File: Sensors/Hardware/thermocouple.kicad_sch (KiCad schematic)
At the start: 8 parts, among them U18 MAX31856

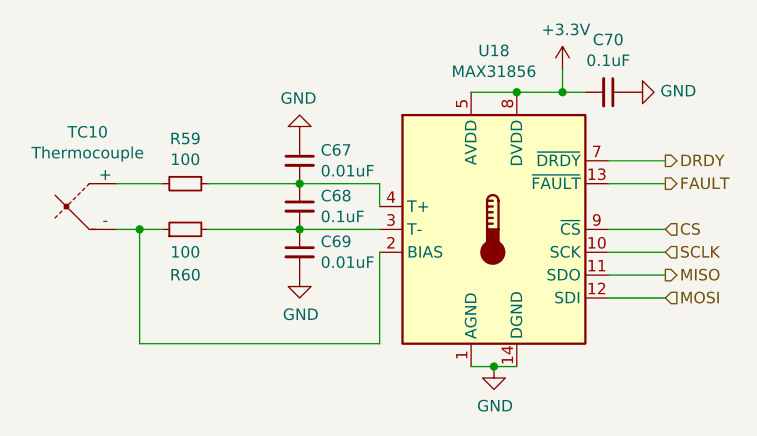
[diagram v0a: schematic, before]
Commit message: added new ADC and some connections
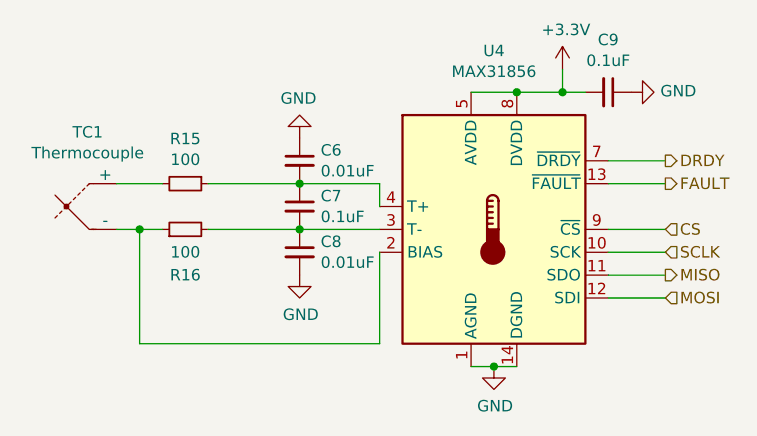
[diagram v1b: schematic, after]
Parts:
- renumbered C67 to C6, C68 to C7, C69 to C8, C70 to C9, R59 to R15, R60 to R16, TC10 to TC1, U18 to U4
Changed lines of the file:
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@@
   (symbol (lib_id "Sensor_Temperature:MAX31856") (at 95.25 73.66 0)
     (in_bom yes) (on_board yes)
-    (property "Reference" "U18" (id 0) (at 95.25 53.8226 0))
+    (property "Reference" "U4" (id 0) (at 95.25 53.8226 0))
     (property "Value" "MAX31856" (id 1) (at 95.25 56.134 0))
     (property "Footprint" "Package_SO:TSSOP-14_4.4x5mm_P0.65mm" (id 2) (at 99.06 87.63 0)
@@
   (symbol (lib_id "power:GND") (at 95.25 88.9 0)
     (in_bom yes) (on_board yes)
-    (property "Reference" "#PWR0130" (id 0) (at 95.25 95.25 0)
+    (property "Reference" "#PWR026" (id 0) (at 95.25 95.25 0)
       (effects (font (size 1.27 1.27)) hide)
     )
@@
   (symbol (lib_id "analogue-cache:+3.3V") (at 102.87 55.88 0)
     (in_bom yes) (on_board yes)
-    (property "Reference" "#PWR0131" (id 0) (at 102.87 59.69 0)
+    (property "Reference" "#PWR028" (id 0) (at 102.87 59.69 0)
       (effects (font (size 1.27 1.27)) hide)
     )
@@
   (symbol (lib_id "Device:C_Small") (at 107.95 58.42 270)
     (in_bom yes) (on_board yes)
-    (property "Reference" "C70" (id 0) (at 107.95 52.6034 90))
+    (property "Reference" "C9" (id 0) (at 107.95 52.6034 90))
     (property "Value" "0.1uF" (id 1) (at 107.95 54.9148 90))
     (property "Footprint" "Capacitor_SMD:C_0603_1608Metric" (id 2) (at 107.95 58.42 0)
@@
   (symbol (lib_id "power:GND") (at 110.49 58.42 90)
     (in_bom yes) (on_board yes)
-    (property "Reference" "#PWR0132" (id 0) (at 116.84 58.42 0)
+    (property "Reference" "#PWR029" (id 0) (at 116.84 58.42 0)
       (effects (font (size 1.27 1.27)) hide)
     )
@@
   (symbol (lib_id "Device:Thermocouple") (at 50.8 71.12 0)
     (in_bom yes) (on_board yes)
-    (property "Reference" "TC10" (id 0) (at 50.1142 62.865 0))
+    (property "Reference" "TC1" (id 0) (at 50.1142 62.865 0))
     (property "Value" "Thermocouple" (id 1) (at 50.1142 65.1764 0))
     (property "Footprint" "TerminalBlock_TE-Connectivity:TerminalBlock_TE_282834-2_1x02_P2.54mm_Horizontal" (id 2) (at 36.195 69.85 0)
@@
   (symbol (lib_id "Device:R_Small") (at 60.96 68.58 270)
     (in_bom yes) (on_board yes)
-    (property "Reference" "R59" (id 0) (at 60.96 63.6016 90))
+    (property "Reference" "R15" (id 0) (at 60.96 63.6016 90))
     (property "Value" "100" (id 1) (at 60.96 65.913 90))
     (property "Footprint" "Resistor_SMD:R_0603_1608Metric" (id 2) (at 60.96 68.58 0)
@@
   (symbol (lib_id "Device:R_Small") (at 60.96 73.66 90)
     (in_bom yes) (on_board yes)
-    (property "Reference" "R60" (id 0) (at 60.96 78.74 90))
+    (property "Reference" "R16" (id 0) (at 60.96 78.74 90))
     (property "Value" "100" (id 1) (at 60.96 76.2 90))
     (property "Footprint" "Resistor_SMD:R_0603_1608Metric" (id 2) (at 60.96 73.66 0)
@@
   (symbol (lib_id "Device:C_Small") (at 73.66 71.12 0)
     (in_bom yes) (on_board yes)
-    (property "Reference" "C68" (id 0) (at 75.9968 69.9516 0)
+    (property "Reference" "C7" (id 0) (at 75.9968 69.9516 0)
       (effects (font (size 1.27 1.27)) (justify left))
     )
@@
   (symbol (lib_id "Device:C_Small") (at 73.66 66.04 0)
     (in_bom yes) (on_board yes)
-    (property "Reference" "C67" (id 0) (at 75.9968 64.8716 0)
+    (property "Reference" "C6" (id 0) (at 75.9968 64.8716 0)
       (effects (font (size 1.27 1.27)) (justify left))
     )
@@
   (symbol (lib_id "Device:C_Small") (at 73.66 76.2 0)
     (in_bom yes) (on_board yes)
-    (property "Reference" "C69" (id 0) (at 75.9968 75.0316 0)
+    (property "Reference" "C8" (id 0) (at 75.9968 75.0316 0)
       (effects (font (size 1.27 1.27)) (justify left))
     )
@@
   (symbol (lib_id "power:GND") (at 73.66 78.74 0)
     (in_bom yes) (on_board yes)
-    (property "Reference" "#PWR0129" (id 0) (at 73.66 85.09 0)
+    (property "Reference" "#PWR025" (id 0) (at 73.66 85.09 0)
       (effects (font (size 1.27 1.27)) hide)
     )
@@
   (symbol (lib_id "power:GND") (at 73.66 63.5 180)
     (in_bom yes) (on_board yes)
-    (property "Reference" "#PWR0128" (id 0) (at 73.66 57.15 0)
+    (property "Reference" "#PWR024" (id 0) (at 73.66 57.15 0)
       (effects (font (size 1.27 1.27)) hide)
     )

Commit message: connectors and update
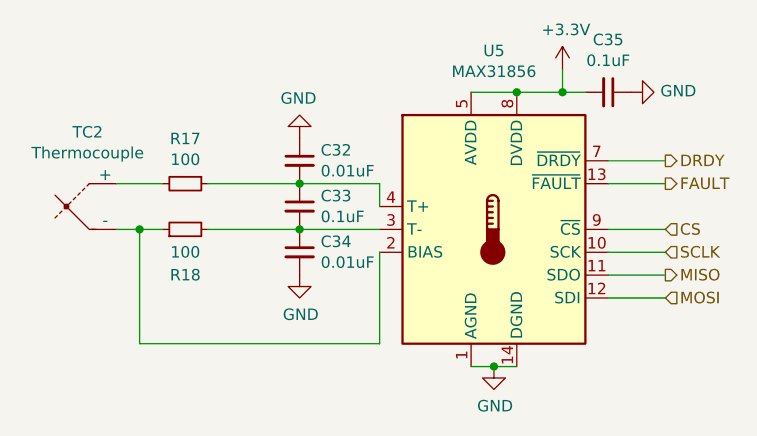
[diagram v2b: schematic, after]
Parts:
- renumbered C6 to C32, C7 to C33, C8 to C34, C9 to C35, R15 to R17, R16 to R18, TC1 to TC2, U4 to U5
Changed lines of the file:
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@@
   (symbol (lib_id "Sensor_Temperature:MAX31856") (at 95.25 73.66 0)
     (in_bom yes) (on_board yes)
-    (property "Reference" "U4" (id 0) (at 95.25 53.8226 0))
+    (property "Reference" "U5" (id 0) (at 95.25 53.8226 0))
     (property "Value" "MAX31856" (id 1) (at 95.25 56.134 0))
     (property "Footprint" "Package_SO:TSSOP-14_4.4x5mm_P0.65mm" (id 2) (at 99.06 87.63 0)
@@
   (symbol (lib_id "power:GND") (at 95.25 88.9 0)
     (in_bom yes) (on_board yes)
-    (property "Reference" "#PWR026" (id 0) (at 95.25 95.25 0)
+    (property "Reference" "#PWR032" (id 0) (at 95.25 95.25 0)
       (effects (font (size 1.27 1.27)) hide)
     )
@@
   (symbol (lib_id "analogue-cache:+3.3V") (at 102.87 55.88 0)
     (in_bom yes) (on_board yes)
-    (property "Reference" "#PWR028" (id 0) (at 102.87 59.69 0)
+    (property "Reference" "#PWR033" (id 0) (at 102.87 59.69 0)
       (effects (font (size 1.27 1.27)) hide)
     )
@@
   (symbol (lib_id "Device:C_Small") (at 107.95 58.42 270)
     (in_bom yes) (on_board yes)
-    (property "Reference" "C9" (id 0) (at 107.95 52.6034 90))
+    (property "Reference" "C35" (id 0) (at 107.95 52.6034 90))
     (property "Value" "0.1uF" (id 1) (at 107.95 54.9148 90))
     (property "Footprint" "Capacitor_SMD:C_0603_1608Metric" (id 2) (at 107.95 58.42 0)
@@
   (symbol (lib_id "power:GND") (at 110.49 58.42 90)
     (in_bom yes) (on_board yes)
-    (property "Reference" "#PWR029" (id 0) (at 116.84 58.42 0)
+    (property "Reference" "#PWR034" (id 0) (at 116.84 58.42 0)
       (effects (font (size 1.27 1.27)) hide)
     )
@@
   (symbol (lib_id "Device:Thermocouple") (at 50.8 71.12 0)
     (in_bom yes) (on_board yes)
-    (property "Reference" "TC1" (id 0) (at 50.1142 62.865 0))
+    (property "Reference" "TC2" (id 0) (at 50.1142 62.865 0))
     (property "Value" "Thermocouple" (id 1) (at 50.1142 65.1764 0))
     (property "Footprint" "TerminalBlock_TE-Connectivity:TerminalBlock_TE_282834-2_1x02_P2.54mm_Horizontal" (id 2) (at 36.195 69.85 0)
@@
   (symbol (lib_id "Device:R_Small") (at 60.96 68.58 270)
     (in_bom yes) (on_board yes)
-    (property "Reference" "R15" (id 0) (at 60.96 63.6016 90))
+    (property "Reference" "R17" (id 0) (at 60.96 63.6016 90))
     (property "Value" "100" (id 1) (at 60.96 65.913 90))
     (property "Footprint" "Resistor_SMD:R_0603_1608Metric" (id 2) (at 60.96 68.58 0)
@@
   (symbol (lib_id "Device:R_Small") (at 60.96 73.66 90)
     (in_bom yes) (on_board yes)
-    (property "Reference" "R16" (id 0) (at 60.96 78.74 90))
+    (property "Reference" "R18" (id 0) (at 60.96 78.74 90))
     (property "Value" "100" (id 1) (at 60.96 76.2 90))
     (property "Footprint" "Resistor_SMD:R_0603_1608Metric" (id 2) (at 60.96 73.66 0)
@@
   (symbol (lib_id "Device:C_Small") (at 73.66 71.12 0)
     (in_bom yes) (on_board yes)
-    (property "Reference" "C7" (id 0) (at 75.9968 69.9516 0)
+    (property "Reference" "C33" (id 0) (at 75.9968 69.9516 0)
       (effects (font (size 1.27 1.27)) (justify left))
     )
@@
   (symbol (lib_id "Device:C_Small") (at 73.66 66.04 0)
     (in_bom yes) (on_board yes)
-    (property "Reference" "C6" (id 0) (at 75.9968 64.8716 0)
+    (property "Reference" "C32" (id 0) (at 75.9968 64.8716 0)
       (effects (font (size 1.27 1.27)) (justify left))
     )
@@
   (symbol (lib_id "Device:C_Small") (at 73.66 76.2 0)
     (in_bom yes) (on_board yes)
-    (property "Reference" "C8" (id 0) (at 75.9968 75.0316 0)
+    (property "Reference" "C34" (id 0) (at 75.9968 75.0316 0)
       (effects (font (size 1.27 1.27)) (justify left))
     )
@@
   (symbol (lib_id "power:GND") (at 73.66 78.74 0)
     (in_bom yes) (on_board yes)
-    (property "Reference" "#PWR025" (id 0) (at 73.66 85.09 0)
+    (property "Reference" "#PWR031" (id 0) (at 73.66 85.09 0)
       (effects (font (size 1.27 1.27)) hide)
     )
@@
   (symbol (lib_id "power:GND") (at 73.66 63.5 180)
     (in_bom yes) (on_board yes)
-    (property "Reference" "#PWR024" (id 0) (at 73.66 57.15 0)
+    (property "Reference" "#PWR030" (id 0) (at 73.66 57.15 0)
       (effects (font (size 1.27 1.27)) hide)
     )

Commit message: potential divider preliminary
for connectors
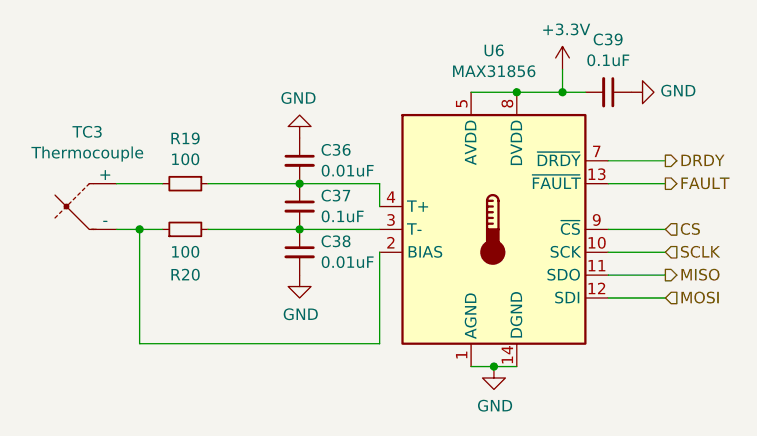
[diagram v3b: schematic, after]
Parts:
- renumbered C32 to C36, C33 to C37, C34 to C38, C35 to C39, R17 to R19, R18 to R20, TC2 to TC3, U5 to U6
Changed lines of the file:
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@@
   (symbol (lib_id "Sensor_Temperature:MAX31856") (at 95.25 73.66 0)
     (in_bom yes) (on_board yes)
-    (property "Reference" "U5" (id 0) (at 95.25 53.8226 0))
+    (property "Reference" "U6" (id 0) (at 95.25 53.8226 0))
     (property "Value" "MAX31856" (id 1) (at 95.25 56.134 0))
     (property "Footprint" "Package_SO:TSSOP-14_4.4x5mm_P0.65mm" (id 2) (at 99.06 87.63 0)
@@
   (symbol (lib_id "power:GND") (at 95.25 88.9 0)
     (in_bom yes) (on_board yes)
-    (property "Reference" "#PWR032" (id 0) (at 95.25 95.25 0)
+    (property "Reference" "#PWR037" (id 0) (at 95.25 95.25 0)
       (effects (font (size 1.27 1.27)) hide)
     )
@@
   (symbol (lib_id "analogue-cache:+3.3V") (at 102.87 55.88 0)
     (in_bom yes) (on_board yes)
-    (property "Reference" "#PWR033" (id 0) (at 102.87 59.69 0)
+    (property "Reference" "#PWR038" (id 0) (at 102.87 59.69 0)
       (effects (font (size 1.27 1.27)) hide)
     )
@@
   (symbol (lib_id "Device:C_Small") (at 107.95 58.42 270)
     (in_bom yes) (on_board yes)
-    (property "Reference" "C35" (id 0) (at 107.95 52.6034 90))
+    (property "Reference" "C39" (id 0) (at 107.95 52.6034 90))
     (property "Value" "0.1uF" (id 1) (at 107.95 54.9148 90))
     (property "Footprint" "Capacitor_SMD:C_0603_1608Metric" (id 2) (at 107.95 58.42 0)
@@
   (symbol (lib_id "power:GND") (at 110.49 58.42 90)
     (in_bom yes) (on_board yes)
-    (property "Reference" "#PWR034" (id 0) (at 116.84 58.42 0)
+    (property "Reference" "#PWR039" (id 0) (at 116.84 58.42 0)
       (effects (font (size 1.27 1.27)) hide)
     )
@@
   (symbol (lib_id "Device:Thermocouple") (at 50.8 71.12 0)
     (in_bom yes) (on_board yes)
-    (property "Reference" "TC2" (id 0) (at 50.1142 62.865 0))
+    (property "Reference" "TC3" (id 0) (at 50.1142 62.865 0))
     (property "Value" "Thermocouple" (id 1) (at 50.1142 65.1764 0))
     (property "Footprint" "TerminalBlock_TE-Connectivity:TerminalBlock_TE_282834-2_1x02_P2.54mm_Horizontal" (id 2) (at 36.195 69.85 0)
@@
   (symbol (lib_id "Device:R_Small") (at 60.96 68.58 270)
     (in_bom yes) (on_board yes)
-    (property "Reference" "R17" (id 0) (at 60.96 63.6016 90))
+    (property "Reference" "R19" (id 0) (at 60.96 63.6016 90))
     (property "Value" "100" (id 1) (at 60.96 65.913 90))
     (property "Footprint" "Resistor_SMD:R_0603_1608Metric" (id 2) (at 60.96 68.58 0)
@@
   (symbol (lib_id "Device:R_Small") (at 60.96 73.66 90)
     (in_bom yes) (on_board yes)
-    (property "Reference" "R18" (id 0) (at 60.96 78.74 90))
+    (property "Reference" "R20" (id 0) (at 60.96 78.74 90))
     (property "Value" "100" (id 1) (at 60.96 76.2 90))
     (property "Footprint" "Resistor_SMD:R_0603_1608Metric" (id 2) (at 60.96 73.66 0)
@@
   (symbol (lib_id "Device:C_Small") (at 73.66 71.12 0)
     (in_bom yes) (on_board yes)
-    (property "Reference" "C33" (id 0) (at 75.9968 69.9516 0)
+    (property "Reference" "C37" (id 0) (at 75.9968 69.9516 0)
       (effects (font (size 1.27 1.27)) (justify left))
     )
@@
   (symbol (lib_id "Device:C_Small") (at 73.66 66.04 0)
     (in_bom yes) (on_board yes)
-    (property "Reference" "C32" (id 0) (at 75.9968 64.8716 0)
+    (property "Reference" "C36" (id 0) (at 75.9968 64.8716 0)
       (effects (font (size 1.27 1.27)) (justify left))
     )
@@
   (symbol (lib_id "Device:C_Small") (at 73.66 76.2 0)
     (in_bom yes) (on_board yes)
-    (property "Reference" "C34" (id 0) (at 75.9968 75.0316 0)
+    (property "Reference" "C38" (id 0) (at 75.9968 75.0316 0)
       (effects (font (size 1.27 1.27)) (justify left))
     )
@@
   (symbol (lib_id "power:GND") (at 73.66 78.74 0)
     (in_bom yes) (on_board yes)
-    (property "Reference" "#PWR031" (id 0) (at 73.66 85.09 0)
+    (property "Reference" "#PWR036" (id 0) (at 73.66 85.09 0)
       (effects (font (size 1.27 1.27)) hide)
     )
@@
   (symbol (lib_id "power:GND") (at 73.66 63.5 180)
     (in_bom yes) (on_board yes)
-    (property "Reference" "#PWR030" (id 0) (at 73.66 57.15 0)
+    (property "Reference" "#PWR035" (id 0) (at 73.66 57.15 0)
       (effects (font (size 1.27 1.27)) hide)
     )

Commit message: fixed hierarchical labels and added ref values
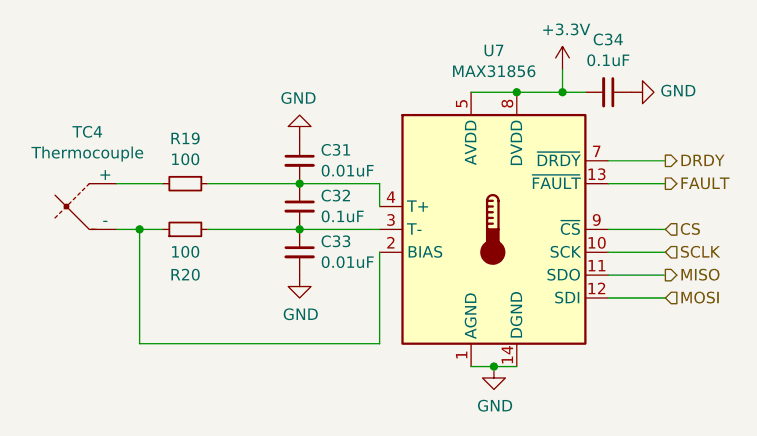
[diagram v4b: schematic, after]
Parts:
- renumbered C36 to C31, C37 to C32, C38 to C33, C39 to C34, TC3 to TC4, U6 to U7
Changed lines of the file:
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@@
   (symbol (lib_id "Sensor_Temperature:MAX31856") (at 95.25 73.66 0)
     (in_bom yes) (on_board yes)
-    (property "Reference" "U6" (id 0) (at 95.25 53.8226 0))
+    (property "Reference" "U7" (id 0) (at 95.25 53.8226 0))
     (property "Value" "MAX31856" (id 1) (at 95.25 56.134 0))
     (property "Footprint" "Package_SO:TSSOP-14_4.4x5mm_P0.65mm" (id 2) (at 99.06 87.63 0)
@@
   (symbol (lib_id "power:GND") (at 95.25 88.9 0)
     (in_bom yes) (on_board yes)
-    (property "Reference" "#PWR037" (id 0) (at 95.25 95.25 0)
+    (property "Reference" "#PWR053" (id 0) (at 95.25 95.25 0)
       (effects (font (size 1.27 1.27)) hide)
     )
@@
   (symbol (lib_id "analogue-cache:+3.3V") (at 102.87 55.88 0)
     (in_bom yes) (on_board yes)
-    (property "Reference" "#PWR038" (id 0) (at 102.87 59.69 0)
+    (property "Reference" "#PWR054" (id 0) (at 102.87 59.69 0)
       (effects (font (size 1.27 1.27)) hide)
     )
@@
   (symbol (lib_id "Device:C_Small") (at 107.95 58.42 270)
     (in_bom yes) (on_board yes)
-    (property "Reference" "C39" (id 0) (at 107.95 52.6034 90))
+    (property "Reference" "C34" (id 0) (at 107.95 52.6034 90))
     (property "Value" "0.1uF" (id 1) (at 107.95 54.9148 90))
     (property "Footprint" "Capacitor_SMD:C_0603_1608Metric" (id 2) (at 107.95 58.42 0)
@@
   (symbol (lib_id "power:GND") (at 110.49 58.42 90)
     (in_bom yes) (on_board yes)
-    (property "Reference" "#PWR039" (id 0) (at 116.84 58.42 0)
+    (property "Reference" "#PWR055" (id 0) (at 116.84 58.42 0)
       (effects (font (size 1.27 1.27)) hide)
     )
@@
   (symbol (lib_id "Device:Thermocouple") (at 50.8 71.12 0)
     (in_bom yes) (on_board yes)
-    (property "Reference" "TC3" (id 0) (at 50.1142 62.865 0))
+    (property "Reference" "TC4" (id 0) (at 50.1142 62.865 0))
     (property "Value" "Thermocouple" (id 1) (at 50.1142 65.1764 0))
     (property "Footprint" "TerminalBlock_TE-Connectivity:TerminalBlock_TE_282834-2_1x02_P2.54mm_Horizontal" (id 2) (at 36.195 69.85 0)
@@
   (symbol (lib_id "Device:C_Small") (at 73.66 71.12 0)
     (in_bom yes) (on_board yes)
-    (property "Reference" "C37" (id 0) (at 75.9968 69.9516 0)
+    (property "Reference" "C32" (id 0) (at 75.9968 69.9516 0)
       (effects (font (size 1.27 1.27)) (justify left))
     )
@@
   (symbol (lib_id "Device:C_Small") (at 73.66 66.04 0)
     (in_bom yes) (on_board yes)
-    (property "Reference" "C36" (id 0) (at 75.9968 64.8716 0)
+    (property "Reference" "C31" (id 0) (at 75.9968 64.8716 0)
       (effects (font (size 1.27 1.27)) (justify left))
     )
@@
   (symbol (lib_id "Device:C_Small") (at 73.66 76.2 0)
     (in_bom yes) (on_board yes)
-    (property "Reference" "C38" (id 0) (at 75.9968 75.0316 0)
+    (property "Reference" "C33" (id 0) (at 75.9968 75.0316 0)
       (effects (font (size 1.27 1.27)) (justify left))
     )
@@
   (symbol (lib_id "power:GND") (at 73.66 78.74 0)
     (in_bom yes) (on_board yes)
-    (property "Reference" "#PWR036" (id 0) (at 73.66 85.09 0)
+    (property "Reference" "#PWR052" (id 0) (at 73.66 85.09 0)
       (effects (font (size 1.27 1.27)) hide)
     )
@@
   (symbol (lib_id "power:GND") (at 73.66 63.5 180)
     (in_bom yes) (on_board yes)
-    (property "Reference" "#PWR035" (id 0) (at 73.66 57.15 0)
+    (property "Reference" "#PWR051" (id 0) (at 73.66 57.15 0)
       (effects (font (size 1.27 1.27)) hide)
     )
